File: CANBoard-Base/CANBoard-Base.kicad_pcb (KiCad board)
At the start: 2 copper layers, 77 parts, among them J1 DTM12 A, J2 DTM12 B, U1 CANBoard_v2, U2 LM324, U3 LM324, U4 SRV05-4, U5 SRV05-4, U6 SRV05-4, U7 SRV05-4, U8 LD1117S33CTR

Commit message: first layout complete
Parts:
- D2, F1, F2, F3, F4, F5, J1, J2: moved to B.Cu
- moved J2 159.5 mm to (-18.4, 18.3), turned to -90 degrees
- moved J1 151.1 mm to (-18.4, -53.6), turned to 90 degrees
- moved R18 90.7 mm to (-0.25, -61.5)
- moved C1 83.0 mm to (-8.13, -39.6), turned to 180 degrees
- moved R17 82.5 mm to (-7.87, -61.5)
- moved R9 80.9 mm to (-6.35, -42.7), turned to 90 degrees
- moved R15 79.9 mm to (-25.4, -61.5), turned to 180 degrees
- moved C2 79.1 mm to (-12.6, -39.6)
- moved C17 78.4 mm to (-42.6, 12.2)
- moved R10 77.4 mm to (-10.7, -42.7), turned to 90 degrees
- moved R19 77.0 mm to (-8.38, -42.7), turned to -90 degrees
- moved C3 75.4 mm to (-17.2, -39.6), turned to 180 degrees
- moved C16 75.2 mm to (-37.1, 12.2), turned to 180 degrees
- moved R20 74.0 mm to (-12.7, -42.7), turned to -90 degrees
- moved R11 73.8 mm to (-15.2, -42.7), turned to 90 degrees
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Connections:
- C3 pad 1: Net-(U4-IO4) -> Net-(U4-IO3)
- C4 pad 1: Net-(U4-IO3) -> Net-(U5-IO1)
- C5 pad 1: Net-(U5-IO1) -> Net-(U5-IO2)
- J1 pad 1: +5VP -> DO4
- J1 pad 2: +5VP -> DO3
- J1 pad 3: DO1 -> DO2
- J1 pad 4: DO2 -> DO1
- J1 pad 5: DO3 -> +5VP
- J1 pad 6: DO4 -> +5VP
- J2 pad 10: DI7_RAW -> DI8_RAW
- J2 pad 11: DI8_RAW -> CANH
- J2 pad 12: GND -> CANL
- J2 pad 2: CANH -> GND
- J2 pad 3: CANL -> DI7_RAW
- J2 pad 4: DI1_RAW -> DI6_RAW
- J2 pad 5: DI2_RAW -> DI3_RAW
- J2 pad 6: DI3_RAW -> DI2_RAW
- J2 pad 7: DI4_RAW -> DI1_RAW
- J2 pad 8: DI5_RAW -> DI4_RAW
- J2 pad 9: DI6_RAW -> DI5_RAW
- R21 pad 2: Net-(U4-IO4) -> Net-(U4-IO3)
- R22 pad 2: Net-(U4-IO3) -> Net-(U5-IO1)
- R23 pad 2: Net-(U5-IO1) -> Net-(U5-IO2)
- R24 pad 2: Net-(U2A-+) -> Net-(U2C-+)
- R26 pad 1: Net-(U4-IO4) -> Net-(U4-IO3)
- R26 pad 2: Net-(U2C-+) -> Net-(U2A-+)
- R27 pad 1: Net-(U4-IO3) -> Net-(U5-IO1)
- R27 pad 2: Net-(U2D-+) -> Net-(U3B-+)
- R28 pad 1: Net-(U5-IO1) -> Net-(U5-IO2)
- R29 pad 1: Net-(U2A-+) -> Net-(U2C-+)
- R31 pad 1: Net-(U2C-+) -> Net-(U2A-+)
- R32 pad 1: Net-(U2D-+) -> Net-(U3B-+)
- U1 pad C5: +5V -> unconnected-(U1-5V-PadC5)
- U1 pad D3: +5V -> unconnected-(U1-5V-PadD3)
- U1 pad D5: +5V -> unconnected-(U1-5V-PadD5)
- U1 pad D7: +5V -> unconnected-(U1-5V-PadD7)
- U2 pad 1: /AnalogInputs/AI1 -> /AnalogInputs/AI3
- U2 pad 12: Net-(U2D-+) -> (no net)
- U2 pad 13: /AnalogInputs/AI4 -> (no net)
- U2 pad 14: /AnalogInputs/AI4 -> (no net)
- U2 pad 2: /AnalogInputs/AI1 -> /AnalogInputs/AI3
- U2 pad 8: /AnalogInputs/AI3 -> /AnalogInputs/AI1
- U2 pad 9: /AnalogInputs/AI3 -> /AnalogInputs/AI1
- U3 pad 5: (no net) -> Net-(U3B-+)
- U3 pad 6: (no net) -> /AnalogInputs/AI4
- U3 pad 7: (no net) -> /AnalogInputs/AI4
- U4 pad 6: Net-(U4-IO4) -> unconnected-(U4-IO4-Pad6)
- U5 pad 3: unconnected-(U5-IO2-Pad3) -> Net-(U5-IO2)
- U6 pad 1: /DigitalInputs/DI5 -> /DigitalInputs/DI6
- U6 pad 3: /DigitalInputs/DI6 -> /DigitalInputs/DI5
- U6 pad 4: /DigitalInputs/DI7 -> /DigitalInputs/DI8
- U6 pad 6: /DigitalInputs/DI8 -> /DigitalInputs/DI7
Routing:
- net +5V: track 0.00 -> 122.6 mm, vias 0 -> 3
- net +3.3V: track 0.00 -> 78.5 mm, vias 0 -> 6
- net Net-(U5-IO1): track 0.00 -> 68.3 mm
- net Net-(U5-IO2): track 0.00 -> 63.3 mm
- net Net-(U4-IO1): track 0.00 -> 61.0 mm, vias 0 -> 2
- net Net-(U4-IO3): track 0.00 -> 53.3 mm
- net Net-(U4-IO2): track 0.00 -> 52.8 mm
- net CANH: track 0.00 -> 37.5 mm
- net /DigitalInputs/DI7: track 0.00 -> 36.9 mm, vias 0 -> 2
- net /DigitalInputs/DI6: track 0.00 -> 35.2 mm, vias 0 -> 2
- net /DigitalInputs/DI3: track 0.00 -> 34.5 mm, vias 0 -> 2
- net /DigitalInputs/DI2: track 0.00 -> 33.9 mm, vias 0 -> 2
- net CANL: track 0.00 -> 33.3 mm
- net +5VP: track 0.00 -> 31.6 mm
- net DO1: track 0.00 -> 31.3 mm
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- added copper zone on B.Cu, net GND
- added copper zone on F.Cu, net GND
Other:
- board outline added: 66.8 x 105.7 mm
- board text added: "1"
- board text added: "2"
- board text added: "3"
- board text added: "4"
- board text added: "5"
- board text added: "PULLDOWN SELECT"
- board text added: "PULLUP SELECT"

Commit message: as built v1
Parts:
- added G1: DingoFace, DRTLogo:DingoFaceNoFill, F.Cu at (-42.7, -51.8)
- D2, F1, F2, F3, F4, F5: moved to F.Cu
- U1: footprint CANBoard:CANBoard_v2_NoMountingHoles -> CANBoard:CANBoard_v2_TagConnectHoles
- moved F2 25.6 mm to (-17.3, -53.6), turned to 90 degrees
- moved F3 24.8 mm to (-20.8, -53.6), turned to 90 degrees
- moved F4 24.3 mm to (-25.1, -53.6), turned to 90 degrees
- moved F5 24.1 mm to (-29.5, -53.6), turned to 90 degrees
- moved D2 6.60 mm to (3.81, -41.9), turned to -90 degrees
- moved F1 6.35 mm to (3.81, -37.5), turned to 90 degrees
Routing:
- net DO1: track 31.3 -> 3.01 mm
- net DO2: track 31.0 -> 2.74 mm
- net DO3: track 30.5 -> 2.79 mm
- net DO4: track 30.2 -> 2.84 mm
- net /DigitalOutputs/DO4_RAW: track 2.75 -> 25.9 mm, vias 0 -> 1
- net /DigitalOutputs/DO1_RAW: track 2.75 -> 25.8 mm, vias 0 -> 1
- net /DigitalOutputs/DO2_RAW: track 2.75 -> 24.8 mm, vias 0 -> 1
- net /DigitalOutputs/DO3_RAW: track 2.85 -> 24.6 mm, vias 0 -> 1
- net +5VP: track 31.6 -> 22.6 mm
- net AI1_RAW: track 19.7 -> 22.7 mm
- net Net-(D2-A): track 3.45 -> 1.81 mm
- net +5V: track 122.6 -> 123.4 mm
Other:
- board text added: "Dingo Electronics CANBoard-Base v1"
- board text added: "PULLDOWN"
- board text added: "PULLUP"
- board text removed: "PULLDOWN SELECT"
- board text removed: "PULLUP SELECT"

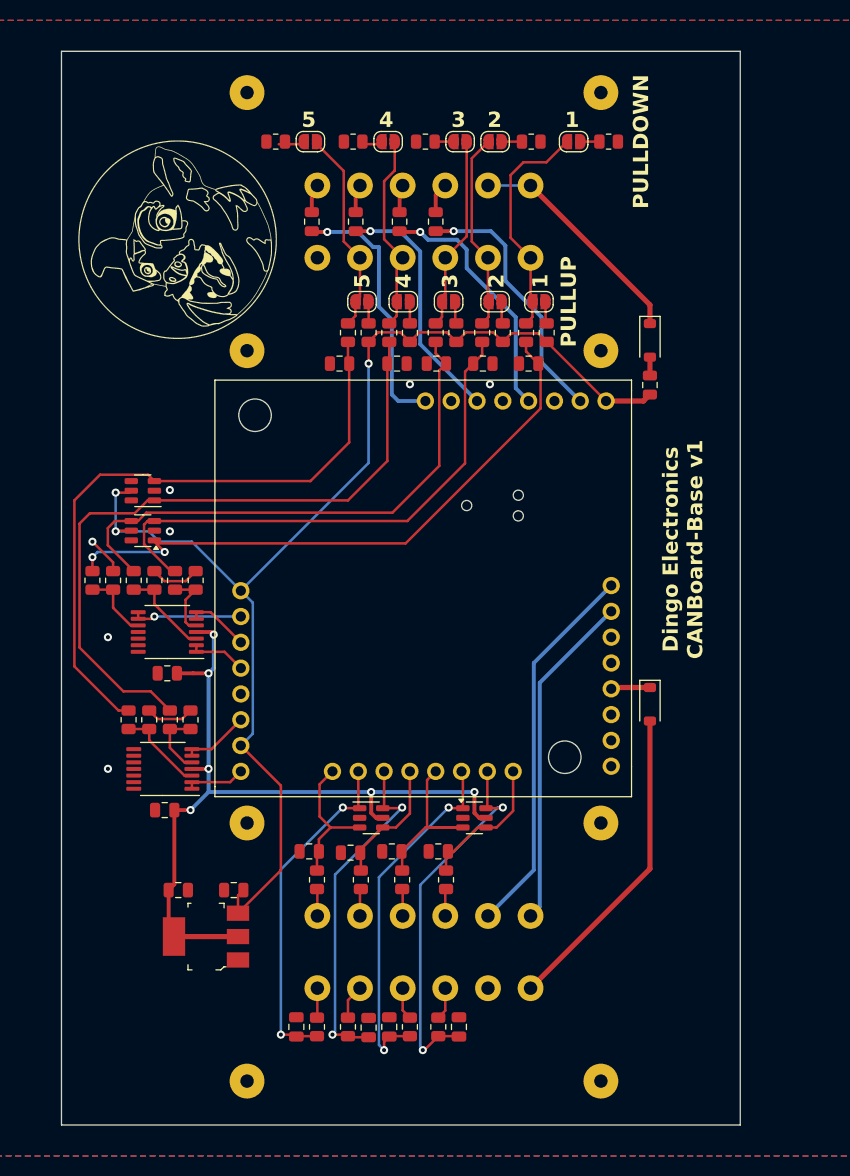
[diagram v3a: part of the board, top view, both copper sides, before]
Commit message: moved dtm connectors together
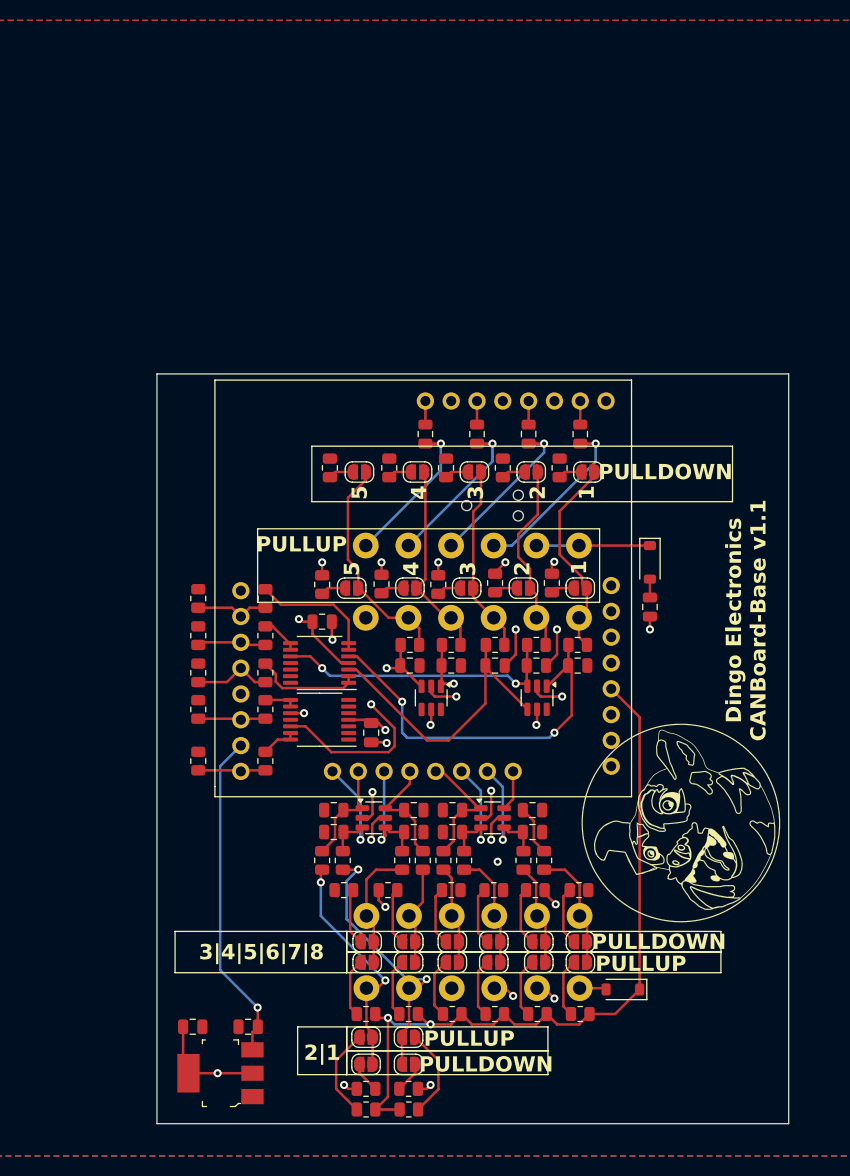
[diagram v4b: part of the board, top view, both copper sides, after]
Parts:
- added JP11: SolderJumper_2_Open, Jumper:SolderJumper-2_P1.3mm_Open_RoundedPad1.0x1.5mm, F.Cu at (-19.9, 26.7)
- added JP12: SolderJumper_2_Open, Jumper:SolderJumper-2_P1.3mm_Open_RoundedPad1.0x1.5mm, F.Cu at (-19.9, 29.3)
- added JP13: SolderJumper_2_Open, Jumper:SolderJumper-2_P1.3mm_Open_RoundedPad1.0x1.5mm, F.Cu at (-24.1, 26.7)
- added JP14: SolderJumper_2_Open, Jumper:SolderJumper-2_P1.3mm_Open_RoundedPad1.0x1.5mm, F.Cu at (-24.1, 29.3)
- added JP15: SolderJumper_2_Open, Jumper:SolderJumper-2_P1.3mm_Open_RoundedPad1.0x1.5mm, F.Cu at (-24.0, 19.3)
- added JP16: SolderJumper_2_Open, Jumper:SolderJumper-2_P1.3mm_Open_RoundedPad1.0x1.5mm, F.Cu at (-24.0, 17.3)
- added JP17: SolderJumper_2_Open, Jumper:SolderJumper-2_P1.3mm_Open_RoundedPad1.0x1.5mm, F.Cu at (-19.9, 19.3)
- added JP18: SolderJumper_2_Open, Jumper:SolderJumper-2_P1.3mm_Open_RoundedPad1.0x1.5mm, F.Cu at (-19.9, 17.3)
- added JP19: SolderJumper_2_Open, Jumper:SolderJumper-2_P1.3mm_Open_RoundedPad1.0x1.5mm, F.Cu at (-15.6, 19.3)
- added JP20: SolderJumper_2_Open, Jumper:SolderJumper-2_P1.3mm_Open_RoundedPad1.0x1.5mm, F.Cu at (-15.6, 17.3)
- added JP21: SolderJumper_2_Open, Jumper:SolderJumper-2_P1.3mm_Open_RoundedPad1.0x1.5mm, F.Cu at (-11.6, 19.3)
- added JP22: SolderJumper_2_Open, Jumper:SolderJumper-2_P1.3mm_Open_RoundedPad1.0x1.5mm, F.Cu at (-11.6, 17.3)
- added JP23: SolderJumper_2_Open, Jumper:SolderJumper-2_P1.3mm_Open_RoundedPad1.0x1.5mm, F.Cu at (-7.13, 19.3)
- added JP24: SolderJumper_2_Open, Jumper:SolderJumper-2_P1.3mm_Open_RoundedPad1.0x1.5mm, F.Cu at (-7.13, 17.3)
- added JP25: SolderJumper_2_Open, Jumper:SolderJumper-2_P1.3mm_Open_RoundedPad1.0x1.5mm, F.Cu at (-3.03, 19.3)
- added JP26: SolderJumper_2_Open, Jumper:SolderJumper-2_P1.3mm_Open_RoundedPad1.0x1.5mm, F.Cu at (-3.03, 17.3)
- added R34: 2.7K, Resistor_SMD:R_0805_2012Metric, F.Cu at (-19.9, 33.8)
- added R35: 2.7K, Resistor_SMD:R_0805_2012Metric, F.Cu at (-19.9, 31.8)
- added R36: 2.7K, Resistor_SMD:R_0805_2012Metric, F.Cu at (-24.1, 33.8)
- added R37: 2.7K, Resistor_SMD:R_0805_2012Metric, F.Cu at (-24.1, 31.8)
- added R38: 2.7K, Resistor_SMD:R_0805_2012Metric, F.Cu at (-24.1, 24.4)
- added R39: 2.7K, Resistor_SMD:R_0805_2012Metric, F.Cu at (-26.3, 12.2)
- added R40: 2.7K, Resistor_SMD:R_0805_2012Metric, F.Cu at (-19.9, 24.4)
- added R41: 2.7K, Resistor_SMD:R_0805_2012Metric, F.Cu at (-22.0, 12.2)
- added R42: 2.7K, Resistor_SMD:R_0805_2012Metric, F.Cu at (-15.6, 24.4)
- added R43: 2.7K, Resistor_SMD:R_0805_2012Metric, F.Cu at (-15.7, 12.2)
- added R44: 2.7K, Resistor_SMD:R_0805_2012Metric, F.Cu at (-11.5, 24.4)
- added R45: 2.7K, Resistor_SMD:R_0805_2012Metric, F.Cu at (-11.6, 12.2)
- added R46: 2.7K, Resistor_SMD:R_0805_2012Metric, F.Cu at (-7.26, 24.4)
- added R47: 2.7K, Resistor_SMD:R_0805_2012Metric, F.Cu at (-7.47, 12.2)
- added R48: 2.7K, Resistor_SMD:R_0805_2012Metric, F.Cu at (-3.05, 24.4)
- added R49: 2.7K, Resistor_SMD:R_0805_2012Metric, F.Cu at (-3.17, 12.2)
- J1, J2: footprint Deutsch_DTM:TE_DTM15-12PA -> Deutsch_DTM:TE_DTM15-12Px_NoScrewHoles
- U1: footprint CANBoard:CANBoard_v2_TagConnectHoles -> CANBoard:CANBoard_v2_NoMountingHoles_TagConnectHoles
- moved G1 75.8 mm to (6.86, 5.59)
- moved U4 42.1 mm to (-7.30, -6.74), turned to -90 degrees
- moved J1 35.8 mm to (-13.7, -18.2)
- moved U5 34.9 mm to (-17.7, -6.73), turned to -90 degrees
- moved JP10 32.9 mm to (-24.8, -29.0)
- moved JP7 32.7 mm to (-7.87, -29.0), turned to 0 degrees
- moved JP9 32.6 mm to (-19.1, -29.0)
- moved R14 32.5 mm to (-27.7, -29.4), turned to 90 degrees
- moved JP6 32.5 mm to (-2.29, -29.0), turned to 0 degrees
- moved JP8 32.5 mm to (-13.5, -29.0)
- moved R18 32.5 mm to (-5.08, -29.4), turned to 90 degrees
- moved R15 32.3 mm to (-21.8, -29.4), turned to 90 degrees
- moved R17 32.2 mm to (-10.7, -29.4), turned to 90 degrees
- moved R16 32.2 mm to (-16.3, -29.4), turned to 90 degrees
- moved R22 31.3 mm to (-15.7, -11.9), turned to 180 degrees
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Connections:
- C1 pad 1: Net-(U4-IO1) -> Net-(U2B-+)
- C14 pad 1: +3.3V -> +5V
- C15 pad 1: +3.3V -> +5V
- C2 pad 1: Net-(U4-IO2) -> Net-(U2C-+)
- C3 pad 1: Net-(U4-IO3) -> Net-(U2A-+)
- C4 pad 1: Net-(U5-IO1) -> Net-(U3C-+)
- C5 pad 1: Net-(U5-IO2) -> Net-(U3D-+)
- J2 pad 10: DI8_RAW -> DI6_RAW
- J2 pad 11: CANH -> DI7_RAW
- J2 pad 12: CANL -> DI8_RAW
- J2 pad 2: GND -> CANL
- J2 pad 3: DI7_RAW -> CANH
- J2 pad 4: DI6_RAW -> GND
- J2 pad 5: DI3_RAW -> DI1_RAW
- J2 pad 7: DI1_RAW -> DI3_RAW
- R19 pad 2: Net-(U4-IO1) -> Net-(U2B-+)
- R20 pad 2: Net-(U4-IO2) -> Net-(U2C-+)
- R21 pad 2: Net-(U4-IO3) -> Net-(U2A-+)
- R22 pad 2: Net-(U5-IO1) -> Net-(U3C-+)
- R23 pad 2: Net-(U5-IO2) -> Net-(U3D-+)
- R24 pad 1: Net-(U4-IO1) -> Net-(U2B--)
- R24 pad 2: Net-(U2C-+) -> /AnalogInputs/AI1
- R25 pad 1: Net-(U4-IO2) -> Net-(U2C--)
- R25 pad 2: Net-(U2B-+) -> /AnalogInputs/AI2
- R26 pad 1: Net-(U4-IO3) -> Net-(U2A--)
- R26 pad 2: Net-(U2A-+) -> /AnalogInputs/AI3
- R27 pad 1: Net-(U5-IO1) -> Net-(U3C--)
- R27 pad 2: Net-(U3B-+) -> /AnalogInputs/AI4
- R28 pad 1: Net-(U5-IO2) -> Net-(U3D--)
- R28 pad 2: Net-(U3A-+) -> /AnalogInputs/AI5
- R29 pad 1: Net-(U2C-+) -> /AnalogInputs/AI1
- R30 pad 1: Net-(U2B-+) -> /AnalogInputs/AI2
- R31 pad 1: Net-(U2A-+) -> /AnalogInputs/AI3
- R32 pad 1: Net-(U3B-+) -> /AnalogInputs/AI4
- R33 pad 1: Net-(U3A-+) -> /AnalogInputs/AI5
- U2 pad 1: /AnalogInputs/AI3 -> Net-(U2A--)
- U2 pad 2: /AnalogInputs/AI3 -> Net-(U2A--)
- U2 pad 4: +3.3V -> +5V
- U2 pad 6: /AnalogInputs/AI2 -> Net-(U2B--)
- U2 pad 7: /AnalogInputs/AI2 -> Net-(U2B--)
- U2 pad 8: /AnalogInputs/AI1 -> Net-(U2C--)
- U2 pad 9: /AnalogInputs/AI1 -> Net-(U2C--)
- U3 pad 1: /AnalogInputs/AI5 -> (no net)
- U3 pad 10: (no net) -> Net-(U3C-+)
- U3 pad 12: (no net) -> Net-(U3D-+)
- U3 pad 13: (no net) -> Net-(U3D--)
- U3 pad 14: (no net) -> Net-(U3D--)
- U3 pad 2: /AnalogInputs/AI5 -> (no net)
- U3 pad 3: Net-(U3A-+) -> (no net)
- U3 pad 4: +3.3V -> +5V
- U3 pad 5: Net-(U3B-+) -> (no net)
- U3 pad 6: /AnalogInputs/AI4 -> (no net)
- U3 pad 7: /AnalogInputs/AI4 -> (no net)
- U3 pad 8: (no net) -> Net-(U3C--)
- U3 pad 9: (no net) -> Net-(U3C--)
- U4 pad 1: Net-(U4-IO1) -> Net-(U2B-+)
- U4 pad 3: Net-(U4-IO2) -> Net-(U2C-+)
- U4 pad 4: Net-(U4-IO3) -> Net-(U2A-+)
- U5 pad 1: Net-(U5-IO1) -> Net-(U3C-+)
- U5 pad 3: Net-(U5-IO2) -> Net-(U3D-+)
- U6 pad 1: /DigitalInputs/DI6 -> /DigitalInputs/DI5
- U6 pad 3: /DigitalInputs/DI5 -> /DigitalInputs/DI6
- U6 pad 4: /DigitalInputs/DI8 -> /DigitalInputs/DI7
- U6 pad 6: /DigitalInputs/DI7 -> /DigitalInputs/DI8
- U7 pad 4: /DigitalInputs/DI4 -> /DigitalInputs/DI3
- U7 pad 6: /DigitalInputs/DI3 -> /DigitalInputs/DI4
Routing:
- net +12V: track 3.86 -> 74.8 mm, vias 0 -> 2
- net +5V: track 123.4 -> 54.9 mm, vias 3 -> 11
- net Net-(U5-IO1): track 68.3 -> 0.00 mm
- net Net-(U5-IO2): track 63.3 -> 0.00 mm
- net Net-(U4-IO1): track 61.0 -> 0.00 mm, vias 2 -> 0
- net Net-(U4-IO3): track 53.3 -> 0.00 mm
- net Net-(U4-IO2): track 52.8 -> 0.00 mm
- net Net-(U2B-+): track 6.83 -> 38.0 mm, vias 0 -> 2
- net Net-(D1-A): track 31.2 -> 2.66 mm
- net Net-(U3D-+): track 0.00 -> 27.2 mm, vias 0 -> 2
- net /DigitalInputs/DI7: track 37.1 -> 12.6 mm, vias 2 -> 1
- net DI1_RAW: track 2.66 -> 27.1 mm, vias 0 -> 2
- net /DigitalOutputs/DO1_RAW: track 25.8 -> 2.32 mm, vias 1 -> 0
- net /DigitalOutputs/DO4_RAW: track 25.9 -> 2.45 mm, vias 1 -> 0
- net /DigitalInputs/DI2: track 33.9 -> 10.6 mm, vias 2 -> 0
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- added copper zone on In1.Cu, net +5V
- added copper zone on In2.Cu, net GND
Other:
- board size 66.8 x 105.7 mm -> 62.2 x 73.8 mm
- copper layers 2 -> 4
- board text added: "2|1"
- board text added: "3|4|5|6|7|8"
- board text added: "Dingo Electronics CANBoard-Base v1.1"
- board text removed: "Dingo Electronics CANBoard-Base v1"
